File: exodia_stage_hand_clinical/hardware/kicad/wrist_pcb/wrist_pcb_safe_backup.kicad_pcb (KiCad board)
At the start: 2 copper layers, 40 x 30 mm, 22 parts, among them J1 USBC_16PIN, J2 ZIF_5PIN, Q1 AO3400A, Q2 2N7002, Q3 2N7002, Q4 2N7002, Q5 2N7002, U1 ESP32S3_MODULE, U2 TP4056_IC, U3 AP2112K

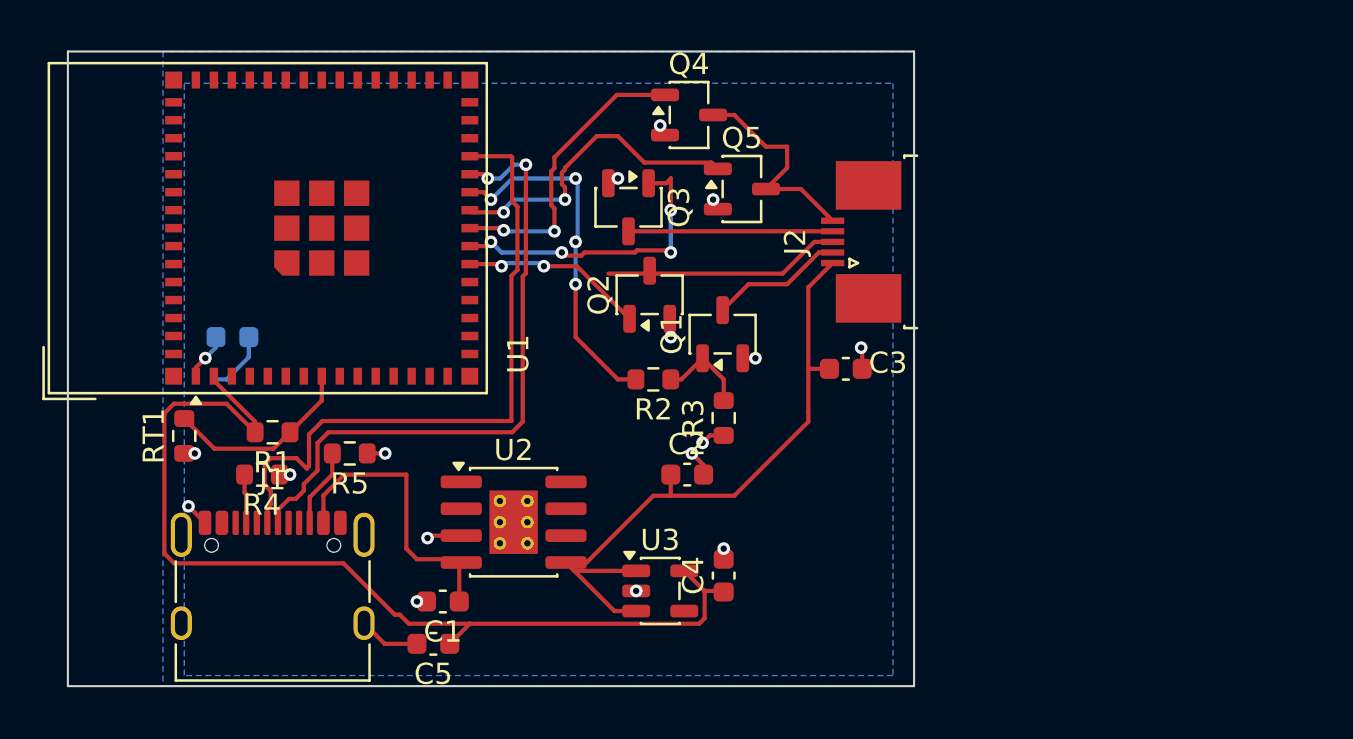
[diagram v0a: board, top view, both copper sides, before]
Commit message: Add Exodia Wrist PCB Rev B and update schematic/layout; clean up .history submodule and optimize .gitignore for KiCad
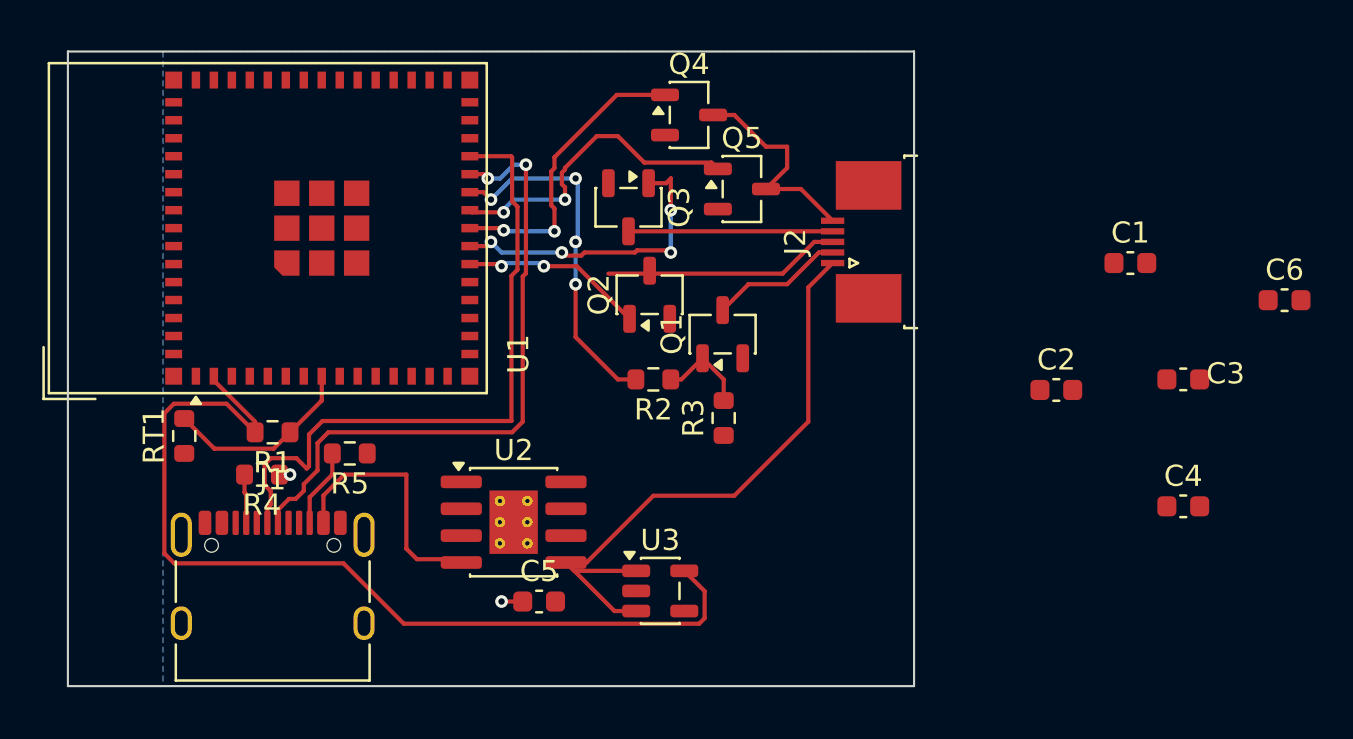
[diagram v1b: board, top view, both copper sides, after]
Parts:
- C6: moved to F.Cu
- moved C6 49.8 mm to (157.5, 111.8), turned to 0 degrees
- moved C1 36.2 mm to (150.2, 110.0), turned to 0 degrees
- moved C4 22.0 mm to (152.7, 121.5), turned to 0 degrees
- moved C2 17.9 mm to (146.7, 116.0)
- moved C3 16.0 mm to (152.7, 115.5)
- moved C5 5.39 mm to (122.3, 126.0), turned to 0 degrees
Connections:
- C1 pad 1: /VBUS -> unconnected-(C1-Pad1)
- C1 pad 2: /GND -> unconnected-(C1-Pad2)
- C2 pad 1: /BAT+ -> unconnected-(C2-Pad1)
- C2 pad 2: /GND -> unconnected-(C2-Pad2)
- C3 pad 1: /BAT+ -> unconnected-(C3-Pad1)
- C3 pad 2: /GND -> unconnected-(C3-Pad2)
- C4 pad 1: /3V3 -> unconnected-(C4-Pad1)
- C4 pad 2: /GND -> unconnected-(C4-Pad2)
- C5 pad 1: /3V3 -> unconnected-(C5-Pad1)
- C5 pad 2: /GND -> unconnected-(C5-Pad2)
- C6 pad 1: /3V3 -> unconnected-(C6-Pad1)
- C6 pad 2: /GND -> unconnected-(C6-Pad2)
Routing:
- net /GND: track 18.2 -> 0.50 mm, vias 17 -> 1
- net /3V3: track 50.0 -> 44.8 mm
- net /BAT+: track 32.3 -> 30.3 mm
- net /VBUS: track 13.9 -> 12.0 mm
- net unconnected-(C5-Pad1): track 0.00 -> 1.00 mm, vias 0 -> 1
